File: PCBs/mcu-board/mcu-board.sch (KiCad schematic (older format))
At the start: 7 parts, among them J1 ENCODER-PANEL-1, J2 ENCODER-PANEL-2, J3 5V, J4 3.3V, J5 MDAC-INPUT-SELECTOR, U1 m0-express

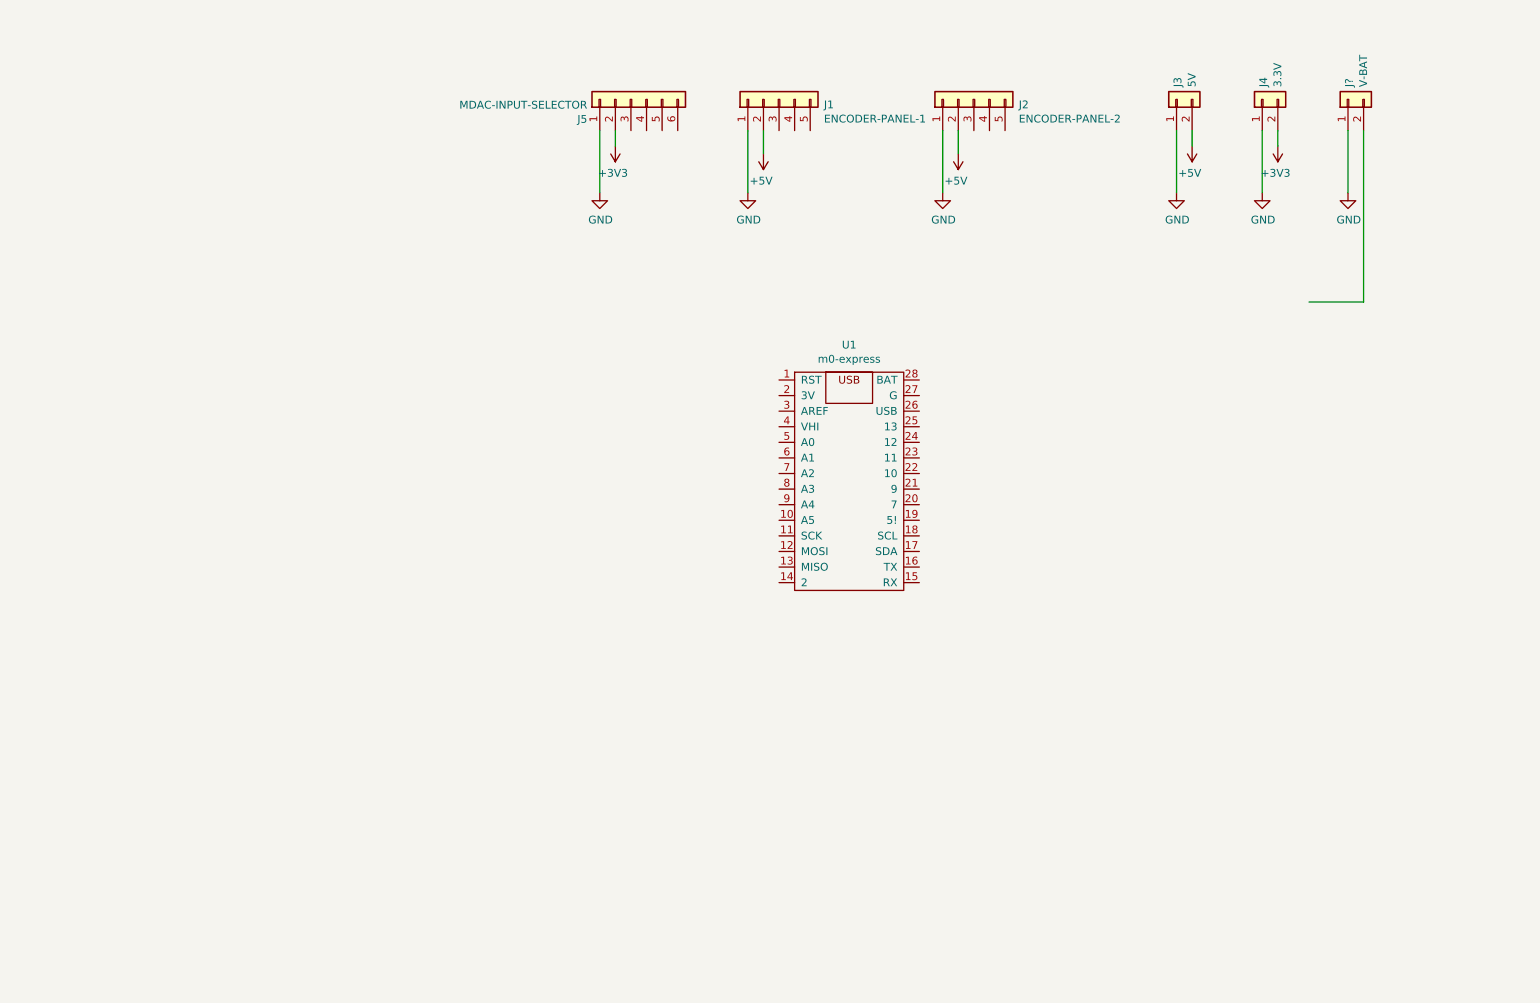
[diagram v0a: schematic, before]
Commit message: Addinng PCB for MCU board (#8)
* Updating mcu-board PCB

* renaming some nets

* starting to fix silkscreen

* change pad/mask clearance

* misc updates

* adding images

* update readme
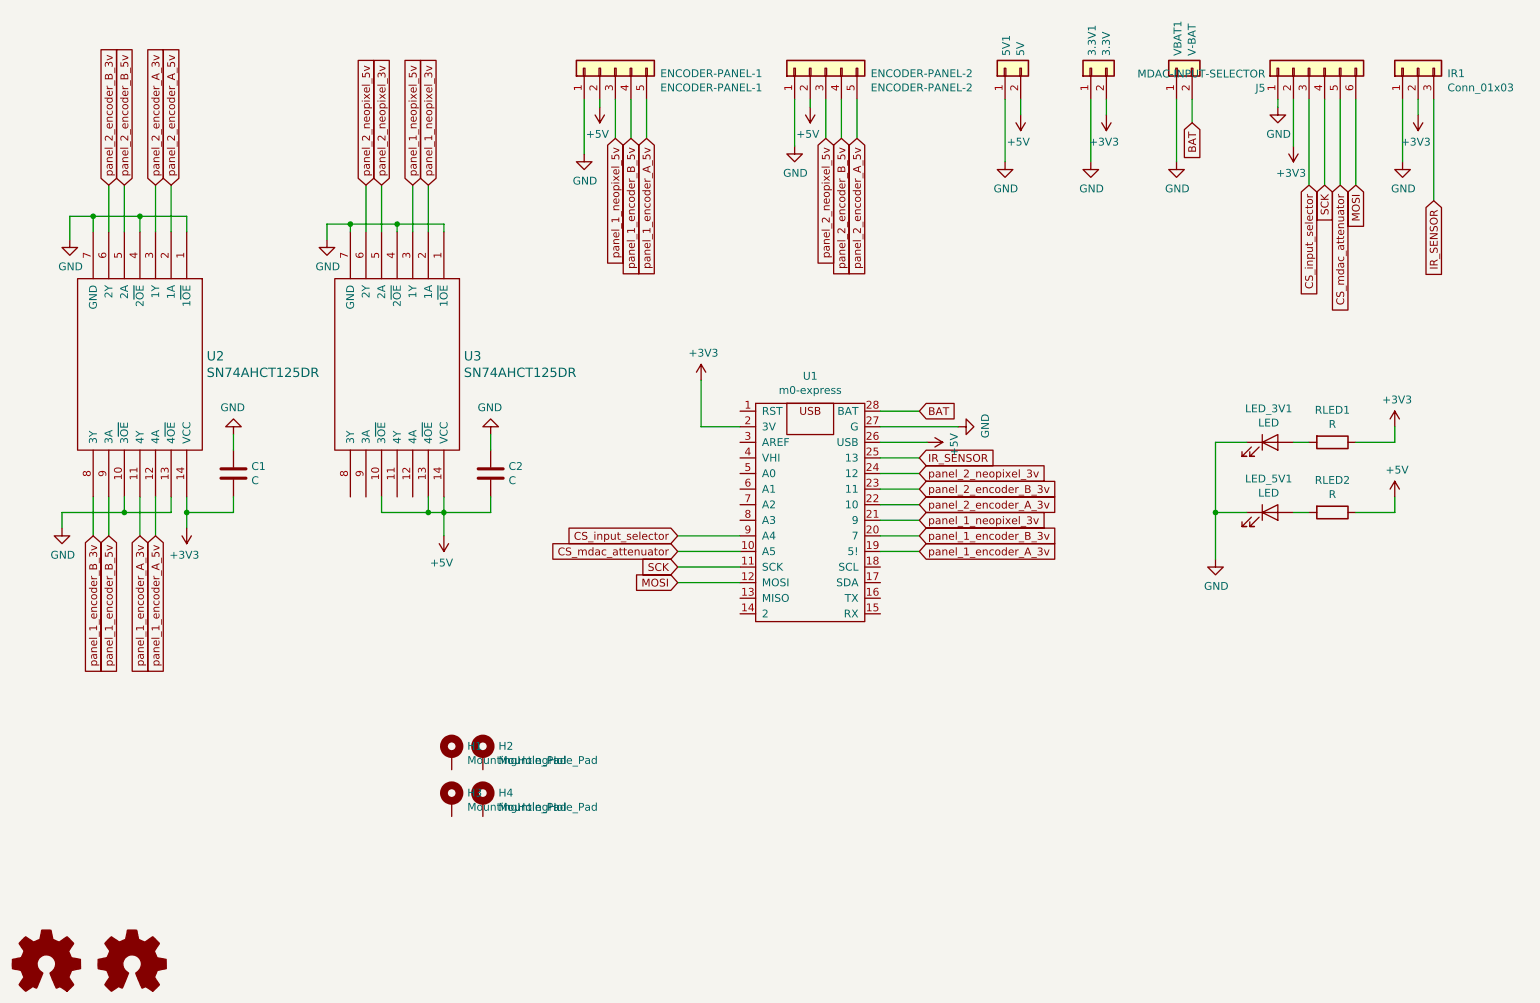
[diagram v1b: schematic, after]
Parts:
- added C1, C2: C, Capacitor_SMD:C_1206_3216Metric_Pad1.42x1.75mm_HandSolder, symbol Device:C
- added H1, H2, H3, H4: MountingHole_Pad, MountingHole:MountingHole_3.2mm_M3_Pad, symbol Mechanical:MountingHole_Pad
- added IR1: Conn_01x03, Connector_Molex:Molex_KK-254_AE-6410-03A_1x03_P2.54mm_Vertical, symbol Connector_Generic:Conn_01x03
- added LED_3V1, LED_5V1: LED, LED_SMD:LED_1206_3216Metric_Pad1.42x1.75mm_HandSolder, symbol Device:LED
- added LOGO1, LOGO2: Logo_Open_Hardware_Small, Symbol:OSHW-Logo2_14.6x12mm_SilkScreen, symbol Graphic:Logo_Open_Hardware_Small
- added RLED1, RLED2: R, Resistor_SMD:R_1206_3216Metric_Pad1.42x1.75mm_HandSolder, symbol Device:R
- added U2, U3: SN74AHCT125DR, Package_SO:SOIC-14_3.9x8.7mm_P1.27mm, symbol SN74AHCT125:SN74AHCT125
- gave numbers to parts that had none: 1
- renumbered J4 to 3.3V1, J3 to 5V1, J1 to ENCODER-PANEL-1, J2 to ENCODER-PANEL-2
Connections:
- net labels added: BAT, CS_input_selector, CS_mdac_attenuator, IR_SENSOR, MOSI, SCK, panel_1_encoder_A_3v, panel_1_encoder_A_5v, panel_1_encoder_B_3v, panel_1_encoder_B_5v, panel_1_neopixel_3v, panel_1_neopixel_5v, panel_2_encoder_A_3v, panel_2_encoder_A_5v, panel_2_encoder_B_3v, panel_2_encoder_B_5v, panel_2_neopixel_3v, panel_2_neopixel_5v
- wire segments 13 -> 96
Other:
- moved on the sheet: 3.3V1, 5V1, ENCODER-PANEL-1, ENCODER-PANEL-2, J5, U1, VBAT1

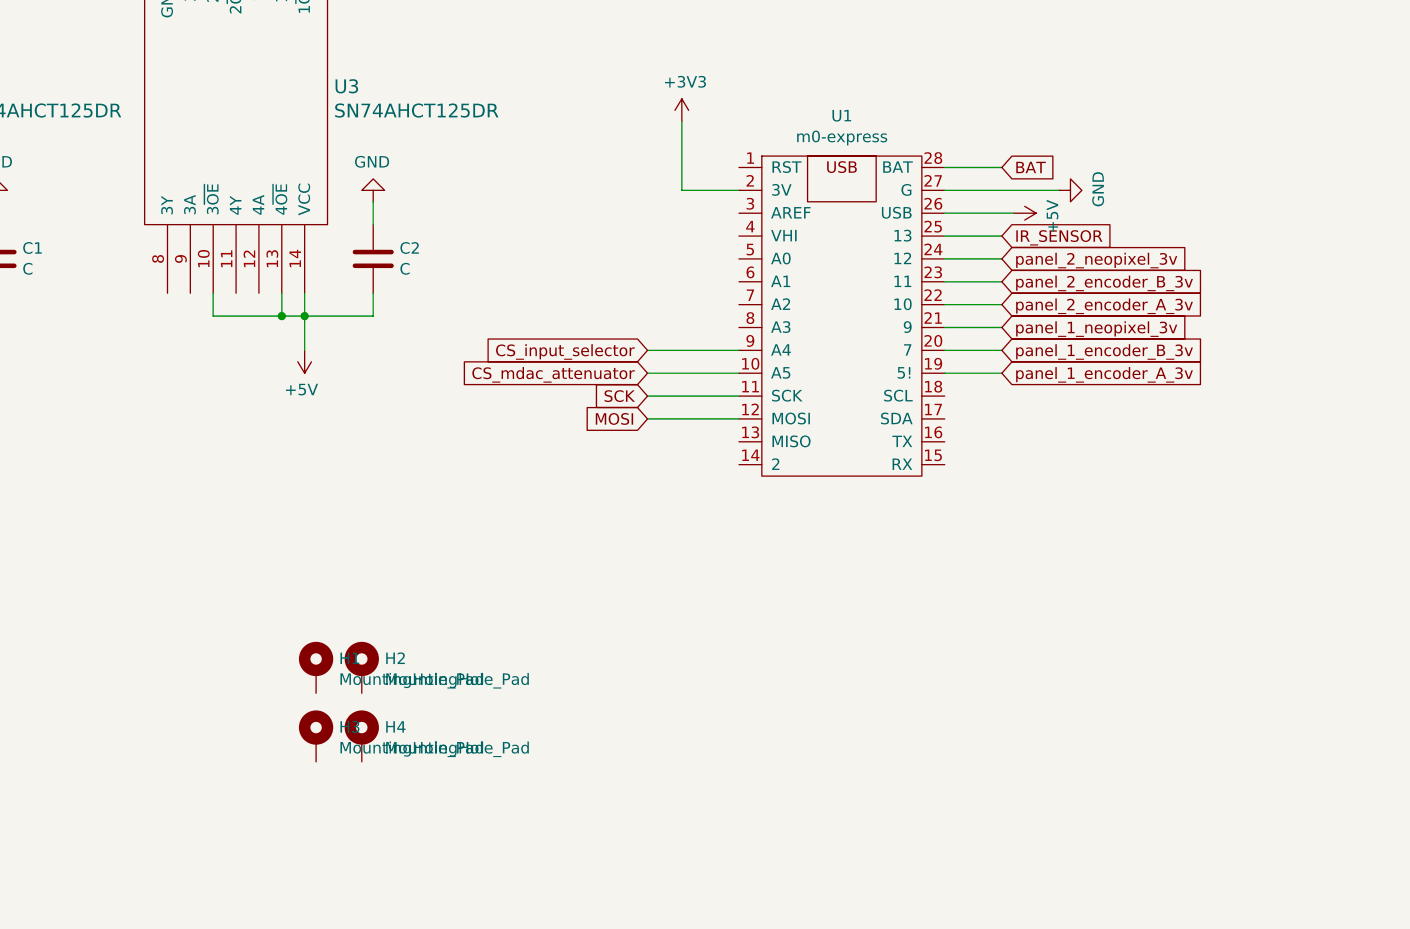
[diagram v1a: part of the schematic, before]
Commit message: Updating mcu-board to not use pin 5
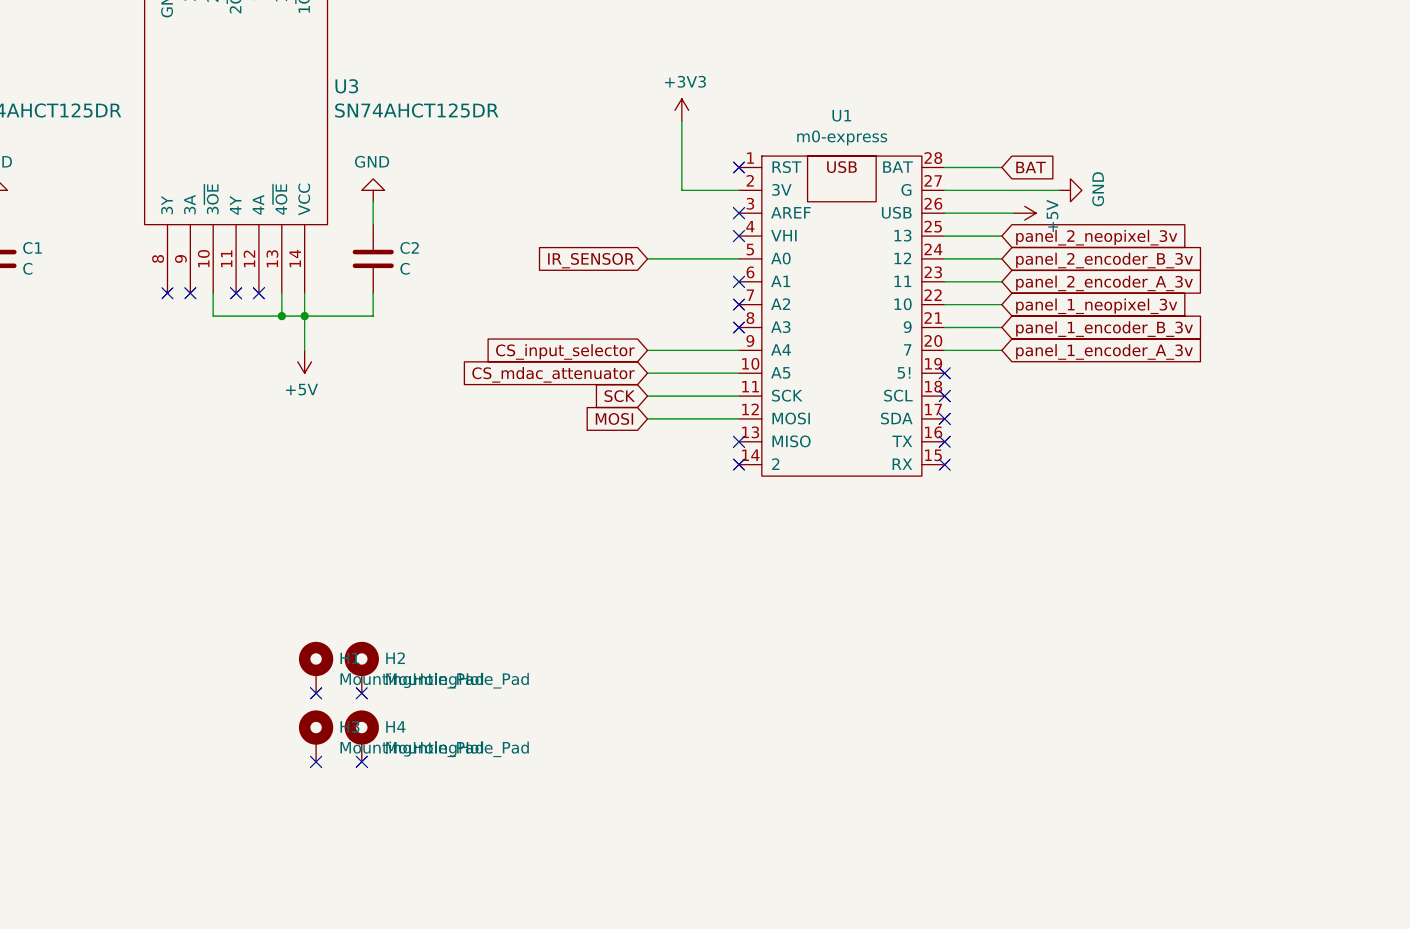
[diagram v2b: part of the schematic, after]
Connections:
- net IR_SENSOR: now also U1.5 (A0); no longer U1.25 (13)
- net panel_1_encoder_A_3v: now also U1.20 (7); no longer U1.19 (5!)
- net panel_1_encoder_B_3v: now also U1.21 (9); no longer U1.20 (7)
- net panel_1_neopixel_3v: now also U1.22 (10); no longer U1.21 (9)
- net panel_2_encoder_A_3v: now also U1.23 (11); no longer U1.22 (10)
- net panel_2_encoder_B_3v: now also U1.24 (12); no longer U1.23 (11)
- net panel_2_neopixel_3v: now also U1.25 (13); no longer U1.24 (12)
- no-connect marks 0 -> 21
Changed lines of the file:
@@
 EESchema Schematic File Version 4
 LIBS:mcu-board-cache
-EELAYER 26 0
+EELAYER 29 0
 EELAYER END
 $Descr A4 11693 8268
@@
 $EndComp
 $Comp
-L adafruit-itsybitsy:m0-express U1
-U 1 1 5C26DA4B
-P 5900 4400
-F 0 "U1" H 5900 5225 50  0000 C CNN
-F 1 "m0-express" H 5900 5134 50  0000 C CNN
-F 2 "m0-express:m0-express" H 5950 4400 50  0001 C CNN
-F 3 "" H 5950 4400 50  0001 C CNN
-	1    5900 4400
-	1    0    0    -1
-$EndComp
-$Comp
 L power:GND #PWR0101
 U 1 1 5C26DC76
@@
 Text GLabel 3150 2350 1    50   Input ~ 0
 panel_2_neopixel_3v
-Text GLabel 6600 4500 2    50   Input ~ 0
+Text GLabel 6600 4400 2    50   Input ~ 0
 panel_1_neopixel_3v
-Text GLabel 6600 4200 2    50   Input ~ 0
+Text GLabel 6600 4100 2    50   Input ~ 0
 panel_2_neopixel_3v
 Text GLabel 3050 2350 1    50   Input ~ 0
@@
 Text GLabel 1700 2350 1    50   Input ~ 0
 panel_2_encoder_A_3v
-Text GLabel 6600 4400 2    50   Input ~ 0
+Text GLabel 6600 4300 2    50   Input ~ 0
 panel_2_encoder_A_3v
-Text GLabel 6600 4300 2    50   Input ~ 0
+Text GLabel 6600 4200 2    50   Input ~ 0
 panel_2_encoder_B_3v
 Text GLabel 1300 4600 3    50   Input ~ 0
@@
 Wire Wire Line
 	1400 4600 1400 4350
-Text GLabel 6600 4700 2    50   Input ~ 0
+Text GLabel 6600 4600 2    50   Input ~ 0
 panel_1_encoder_A_3v
-Text GLabel 6600 4600 2    50   Input ~ 0
+Text GLabel 6600 4500 2    50   Input ~ 0
 panel_1_encoder_B_3v
 $Comp
@@
 Wire Wire Line
 	6350 4600 6600 4600
-Wire Wire Line
-	6350 4700 6600 4700
 Text GLabel 6000 2050 3    50   Input ~ 0
 panel_2_neopixel_5v
@@
 Text GLabel 9900 2450 3    50   Input ~ 0
 IR_SENSOR
-Text GLabel 6600 4100 2    50   Input ~ 0
+Text GLabel 5050 4200 0    50   Input ~ 0
 IR_SENSOR
 Wire Wire Line
@@
 	1    0    0    -1
 $EndComp
+$Comp
+L adafruit-itsybitsy:m0-express U1
+U 1 1 5C9D0D99
+P 5900 4400
+F 0 "U1" H 5900 5225 50  0000 C CNN
+F 1 "m0-express" H 5900 5134 50  0000 C CNN
+F 2 "m0-express:m0-express" H 5950 4400 50  0001 C CNN
+F 3 "" H 5950 4400 50  0001 C CNN
+	1    5900 4400
+	1    0    0    -1
+$EndComp
+Wire Wire Line
+	5050 4200 5450 4200
+NoConn ~ 3350 4350
+NoConn ~ 3250 4350
+NoConn ~ 3050 4350
+NoConn ~ 2950 4350
+NoConn ~ 5450 4500
+NoConn ~ 5450 4400
+NoConn ~ 5450 4300
+NoConn ~ 5450 4100
+NoConn ~ 5450 4000
+NoConn ~ 5450 3800
+NoConn ~ 6350 4700
+NoConn ~ 6350 4800
+NoConn ~ 6350 4900
+NoConn ~ 6350 5000
+NoConn ~ 6350 5100
+NoConn ~ 5450 5100
+NoConn ~ 5450 5000
+NoConn ~ 3600 6100
+NoConn ~ 3800 6100
+NoConn ~ 3800 6400
+NoConn ~ 3600 6400
 $EndSCHEMATC
